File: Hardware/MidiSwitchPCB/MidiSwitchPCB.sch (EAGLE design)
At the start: 78 parts, among them IC3 74LVC2G04GW,125, J1 694108106102, J2 NMJ6HCD2, J3 NMJ6HCD2, J4 NMJ6HCD2, J5 NMJ6HCD2, Q1 BSS123, Q2 BSS123, Q3 BSS123, Q4 BSS123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

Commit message: Continued Layout editing.
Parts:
- C_OUT: device rcl:C-EUC1206 -> rcl:C-EUC1210K
- OK1: value HCPL0500 -> 6N138S; device optocoupler:HCPL0500 -> 6N138S:6N138S
- R20, R21, R22, R23, R24, R25, R26, R27: value (none) -> 61
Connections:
- removed net N$2: U$1.P$1
- removed net N$4: U$1.P$2
- removed net N$6: U$1.P$3
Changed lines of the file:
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@@
 <setting verticaltext="up"/>
 </settings>
-<grid distance="0.01" unitdist="mm" unit="mm" style="lines" multiple="10" display="yes" altdistance="0.01" altunitdist="mm" altunit="mm"/>
+<grid distance="0.01" unitdist="mm" unit="mm" style="lines" multiple="1" display="no" altdistance="0.01" altunitdist="mm" altunit="mm"/>
 <layers>
 <layer number="1" name="Top" color="4" fill="1" visible="no" active="no"/>
@@
 </class>
 <class number="1" name="Power" width="1.016" drill="1.016">
-<clearance class="1" value="0.4064"/>
+<clearance class="1" value="0.8128"/>
 </class>
 <class number="2" name="Signal" width="0.4064" drill="0.6096">
 <clearance class="2" value="0.4064"/>
+</class>
+<class number="3" name="WideIsolation" width="0.4064" drill="1.016">
+<clearance class="3" value="2.032"/>
 </class>
 </classes>
@@
 <part name="U$2" library="MidiSwitchParts" deviceset="MIDI_CONNECTOR" device=""/>
 <part name="U$1" library="MidiSwitchParts" deviceset="MIDI_CONNECTOR" device=""/>
-<part name="OK1" library="optocoupler" deviceset="HCPL0500" device=""/>
+<part name="OK1" library="6N138S" deviceset="6N138S" device=""/>
 <part name="D1" library="diode" deviceset="BAS70" device=""/>
 <part name="R1" library="rcl" deviceset="R-EU_" device="R0603" value="220"/>
@@
 <part name="SUPPLY14" library="supply2" deviceset="GND" device=""/>
 <part name="SUPPLY15" library="supply2" deviceset="GND" device=""/>
-<part name="C_OUT" library="rcl" deviceset="C-EU" device="C1206" value="22µF"/>
+<part name="C_OUT" library="rcl" deviceset="C-EU" device="C1210K" value="22µF"/>
 <part name="SUPPLY16" library="supply2" deviceset="GND" device=""/>
 <part name="C_BST2" library="rcl" deviceset="C-EU" device="C1206" value="100nF"/>
@@
 <part name="R_PWRL_UP" library="rcl" deviceset="R-EU_" device="R0603" value="0R"/>
 <part name="R_PWRL_DOWN" library="rcl" deviceset="R-EU_" device="R0603" value="0R"/>
-<part name="R20" library="rcl" deviceset="R-EU_" device="R0603"/>
-<part name="R21" library="rcl" deviceset="R-EU_" device="R0603"/>
-<part name="R22" library="rcl" deviceset="R-EU_" device="R0603"/>
-<part name="R23" library="rcl" deviceset="R-EU_" device="R0603"/>
-<part name="R24" library="rcl" deviceset="R-EU_" device="R0603"/>
-<part name="R25" library="rcl" deviceset="R-EU_" device="R0603"/>
-<part name="R26" library="rcl" deviceset="R-EU_" device="R0603"/>
-<part name="R27" library="rcl" deviceset="R-EU_" device="R0603"/>
+<part name="R20" library="rcl" deviceset="R-EU_" device="R0603" value="61"/>
+<part name="R21" library="rcl" deviceset="R-EU_" device="R0603" value="61"/>
+<part name="R22" library="rcl" deviceset="R-EU_" device="R0603" value="61"/>
+<part name="R23" library="rcl" deviceset="R-EU_" device="R0603" value="61"/>
+<part name="R24" library="rcl" deviceset="R-EU_" device="R0603" value="61"/>
+<part name="R25" library="rcl" deviceset="R-EU_" device="R0603" value="61"/>
+<part name="R26" library="rcl" deviceset="R-EU_" device="R0603" value="61"/>
+<part name="R27" library="rcl" deviceset="R-EU_" device="R0603" value="61"/>
 <part name="J1" library="SamacSys_Parts" deviceset="694108106102" device=""/>
 <part name="U$3" library="SamacSys_Parts" deviceset="G6L-1F-TR_DC5-NEW" device=""/>
@@
 <instance part="U$2" gate="G$1" x="13.14" y="53.42"/>
 <instance part="U$1" gate="G$1" x="12.5" y="82.6"/>
-<instance part="OK1" gate="A" x="57.82" y="83.54"/>
+<instance part="OK1" gate="G$1" x="57.82" y="83.54"/>
 <instance part="D1" gate="1" x="43.32" y="82.01" rot="R90"/>
 <instance part="R1" gate="G$1" x="37.53" y="88.6"/>
@@
 </busses>
 <nets>
-<net name="N$2" class="0">
-<segment>
-<wire x1="25.5" y1="88.6" x2="27.9" y2="88.6" width="0.1524" layer="91"/>
-<pinref part="U$1" gate="G$1" pin="P$1"/>
-</segment>
-</net>
-<net name="N$4" class="0">
-<segment>
-<wire x1="25.5" y1="82.6" x2="28.1" y2="82.6" width="0.1524" layer="91"/>
-<pinref part="U$1" gate="G$1" pin="P$2"/>
-</segment>
-</net>
-<net name="N$6" class="0">
-<segment>
-<wire x1="25.5" y1="76.6" x2="28.3" y2="76.6" width="0.1524" layer="91"/>
-<pinref part="U$1" gate="G$1" pin="P$3"/>
-</segment>
-</net>
-<net name="N$3" class="0">
+<net name="N$3" class="3">
 <segment>
 <pinref part="U$1" gate="G$1" pin="P$4"/>
@@
 <net name="N$7" class="0">
 <segment>
-<pinref part="OK1" gate="A" pin="A"/>
+<pinref part="OK1" gate="G$1" pin="A"/>
 <wire x1="43.32" y1="84.55" x2="43.34" y2="88.6" width="0.1524" layer="91"/>
 <wire x1="43.34" y1="88.6" x2="45.12" y2="88.62" width="0.1524" layer="91"/>
@@
 </segment>
 </net>
-<net name="N$8" class="0">
+<net name="N$8" class="3">
 <segment>
 <wire x1="45.12" y1="78.46" x2="43.33" y2="78.44" width="0.1524" layer="91"/>
@@
 <wire x1="43.33" y1="78.44" x2="32.82" y2="78.44" width="0.1524" layer="91"/>
 <wire x1="32.82" y1="78.44" x2="31.55" y2="79.56" width="0.1524" layer="91"/>
-<pinref part="OK1" gate="A" pin="C"/>
+<pinref part="OK1" gate="G$1" pin="C"/>
 <junction x="43.33" y="78.44"/>
 <pinref part="D1" gate="1" pin="A"/>
@@
 <net name="MIDI_RX" class="0">
 <segment>
-<pinref part="OK1" gate="A" pin="VB"/>
+<pinref part="OK1" gate="G$1" pin="VB"/>
 <pinref part="R2" gate="G$1" pin="2"/>
-<wire x1="67.98" y1="86.08" x2="80.37" y2="86.07" width="0.1524" layer="91"/>
+<wire x1="70.52" y1="86.08" x2="80.37" y2="86.07" width="0.1524" layer="91"/>
 <wire x1="80.37" y1="86.07" x2="80.37" y2="85.37" width="0.1524" layer="91"/>
 <wire x1="86.48" y1="86.07" x2="80.37" y2="86.07" width="0.1524" layer="91"/>
@@
 <net name="N$9" class="0">
 <segment>
-<pinref part="OK1" gate="A" pin="VO"/>
+<pinref part="OK1" gate="G$1" pin="VO"/>
 <pinref part="R3" gate="G$1" pin="1"/>
-<wire x1="67.98" y1="83.54" x2="75.44" y2="83.54" width="0.1524" layer="91"/>
+<wire x1="70.52" y1="83.54" x2="75.44" y2="83.54" width="0.1524" layer="91"/>
 <wire x1="75.44" y1="83.54" x2="88.47" y2="83.58" width="0.1524" layer="91"/>
 <wire x1="88.47" y1="83.58" x2="103.89" y2="83.58" width="0.1524" layer="91"/>
 <pinref part="CN7" gate="A" pin="3"/>
 <wire x1="103.89" y1="83.58" x2="103.94" y2="93.07" width="0.1524" layer="91"/>
+<junction x="75.44" y="83.54"/>
 </segment>
 </net>
@@
 <wire x1="80.37" y1="75.21" x2="72.64" y2="75.21" width="0.1524" layer="91"/>
 <pinref part="SUPPLY1" gate="GND" pin="GND"/>
-<pinref part="OK1" gate="A" pin="GND"/>
-<wire x1="67.98" y1="78.46" x2="72.64" y2="78.46" width="0.1524" layer="91"/>
+<pinref part="OK1" gate="G$1" pin="GND"/>
+<wire x1="70.52" y1="78.46" x2="72.64" y2="78.46" width="0.1524" layer="91"/>
 <junction x="72.64" y="75.2"/>
 </segment>
@@
 <pinref part="U$1" gate="G$1" pin="P$6"/>
 <pinref part="SUPPLY2" gate="GND" pin="GND"/>
+<junction x="29.5" y="73.61"/>
 </segment>
 <segment>
@@
 <net name="VCC_3_3" class="0">
 <segment>
-<pinref part="OK1" gate="A" pin="VCC"/>
-<wire x1="67.98" y1="88.62" x2="67.98" y2="94.64" width="0.1524" layer="91"/>
+<pinref part="OK1" gate="G$1" pin="VCC"/>
+<wire x1="70.52" y1="88.62" x2="70.46" y2="90.84" width="0.1524" layer="91"/>
 <pinref part="R3" gate="G$1" pin="2"/>
-<wire x1="67.98" y1="94.64" x2="70.52" y2="94.64" width="0.1524" layer="91"/>
+<wire x1="70.46" y1="90.84" x2="70.52" y2="94.64" width="0.1524" layer="91"/>
 <wire x1="70.52" y1="94.64" x2="75.44" y2="94.64" width="0.1524" layer="91"/>
 <wire x1="75.44" y1="94.64" x2="75.44" y2="93.7" width="0.1524" layer="91"/>
@@
 </segment>
 </net>
-<net name="N$66" class="0">
+<net name="N$66" class="1">
 <segment>
 <pinref part="F1" gate="G$1" pin="2"/>
@@
 </sheet>
 </sheets>
+<errors>
+</errors>
 </schematic>
 </drawing>

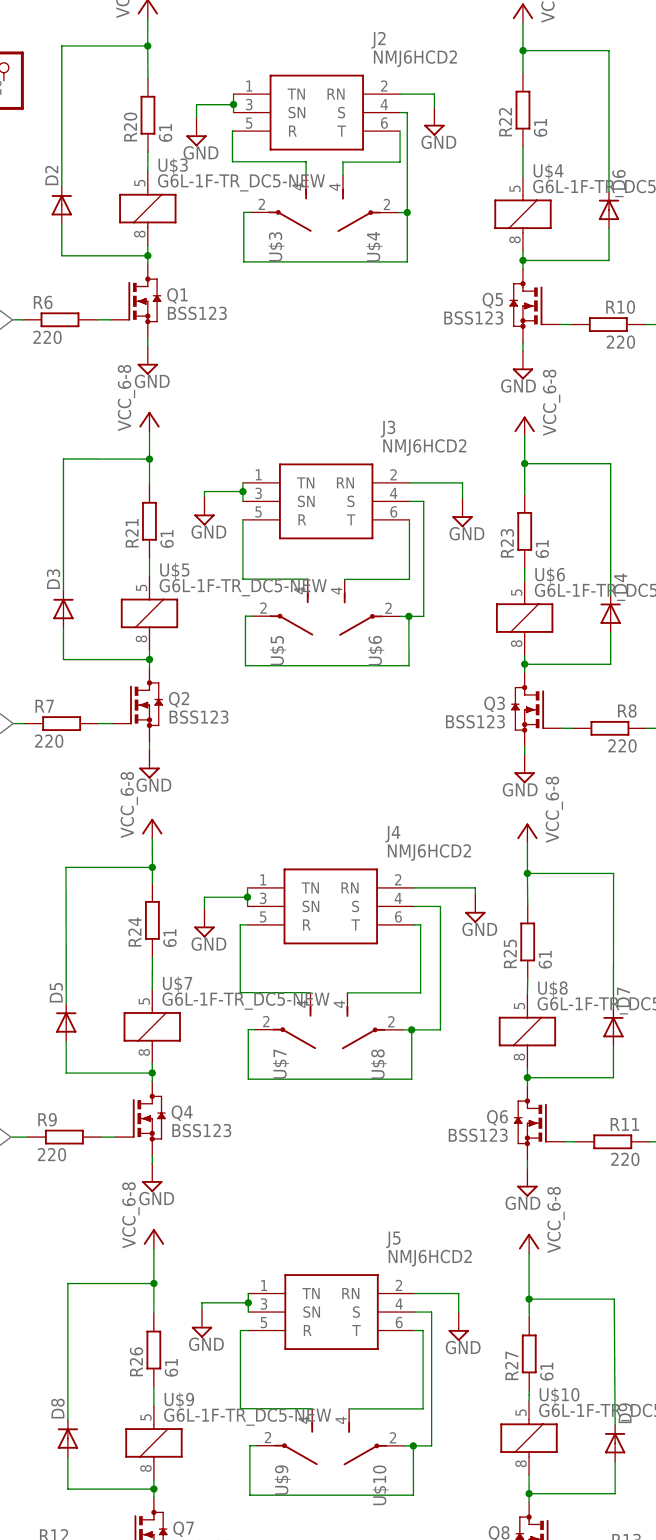
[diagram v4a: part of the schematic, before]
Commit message: Changed PCB size to 160 x 100
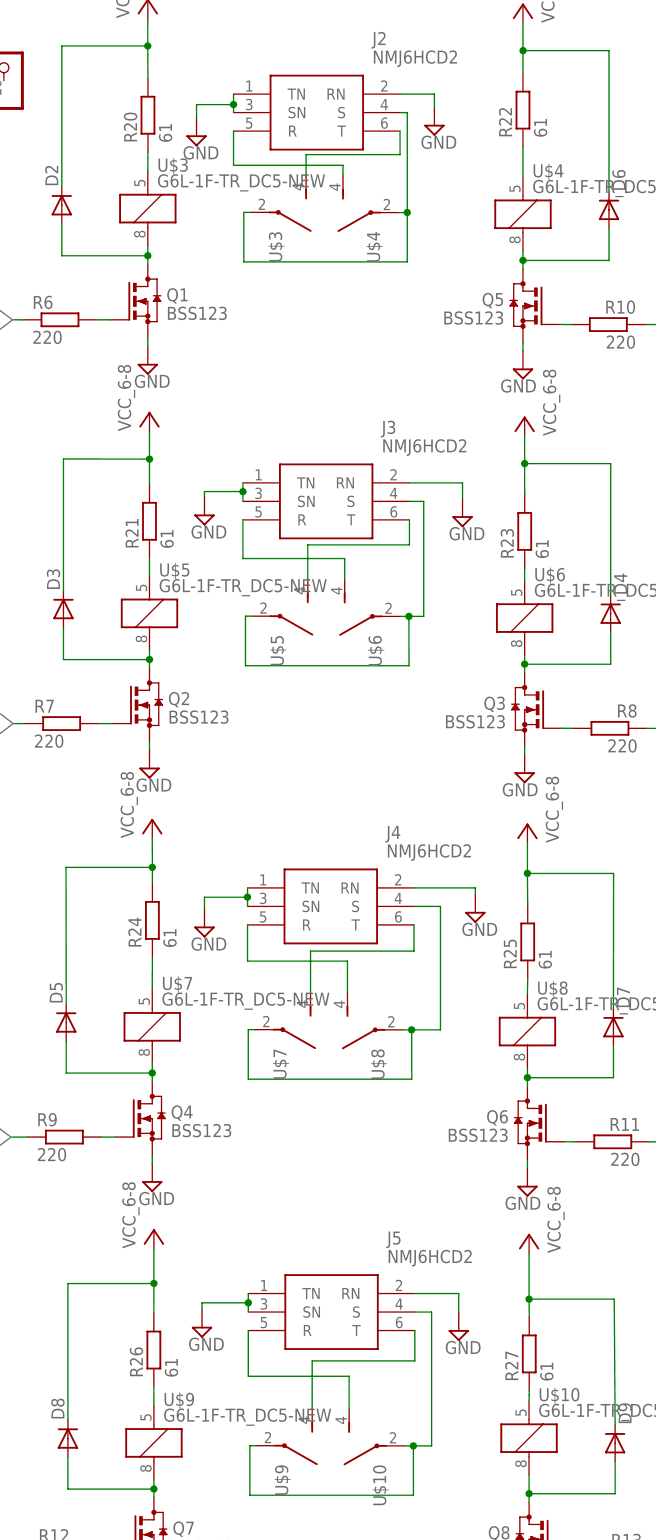
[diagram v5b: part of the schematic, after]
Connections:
- removed net N$36: J2.R, U$3G$2.S
- removed net N$37: J2.T, U$4G$2.S
- removed net N$41: J5.R, U$9G$2.S
- removed net N$50: J5.T, U$10G$2.S
- new net N$2: J2.T, U$3G$2.S
- new net N$28: J4.R, U$8G$2.S
- new net N$4: J2.R, U$4G$2.S
- new net N$6: J3.T, U$5G$2.S
- net N$19: now also U$6G$2.S; no longer U$5G$2.S
- net N$22: now also J4.T, U$7G$2.S; no longer J3.T, U$6G$2.S
- net N$29: now also J5.T, U$9G$2.S; no longer J4.T, U$8G$2.S
- net N$30: now also J5.R, U$10G$2.S; no longer J4.R, U$7G$2.S

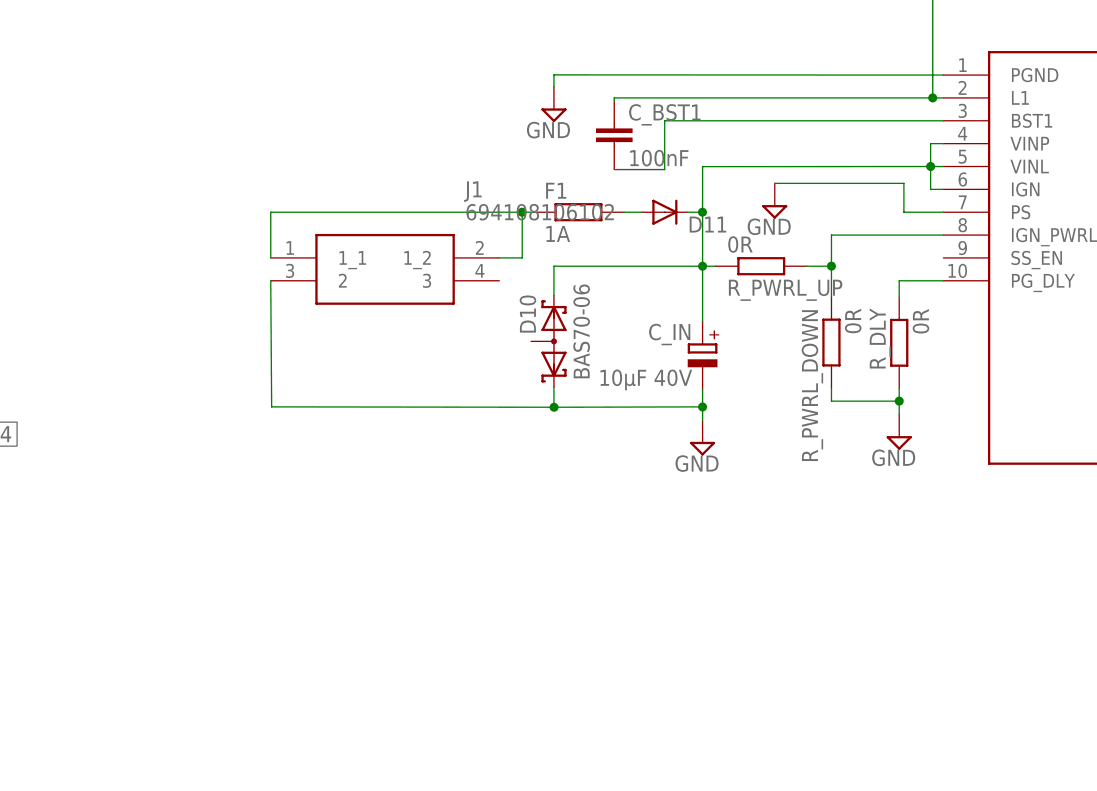
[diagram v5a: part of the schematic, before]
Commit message: Started reworking the layout before ordering it
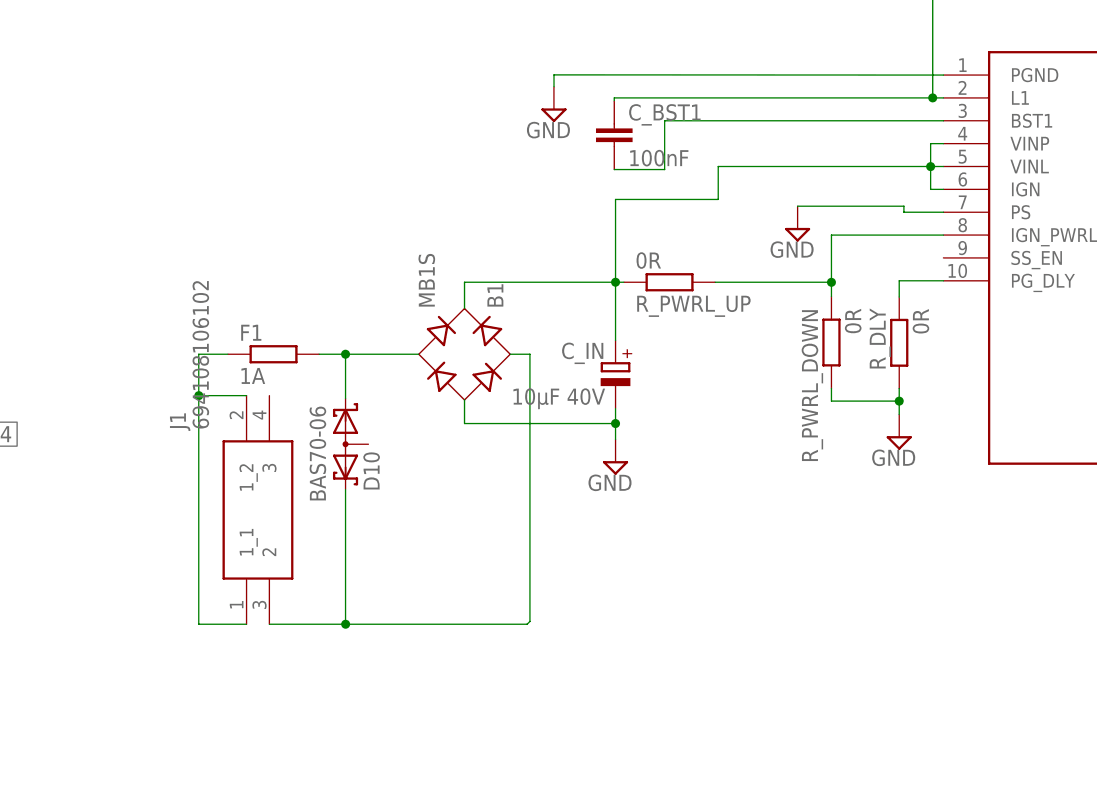
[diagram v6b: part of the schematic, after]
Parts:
- removed D11: (no value), diode:DIODE-DO-214AC
- added B1: MB1S, rectifier:MB1S
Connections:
- removed net N$66: D11.A, F1.2
- removed net VIN: F1.1, J1.1_1
- removed net VIN_FUSED: C_IN.+, D10.K2, D11.C, PS1.IGN, PS1.VINL, PS1.VINP, R_PWRL_UP.1
- new net N$36: B1.AC2, D10.K1, F1.2
- new net N$37: B1.AC1, D10.K2, J1.2
- new net N$40: F1.1, J1.1_1, J1.1_2
- new net N$41: B1.+, C_IN.+, PS1.IGN, PS1.VINL, PS1.VINP, R_PWRL_UP.1
- net GND: now also B1.-; no longer D10.K1, J1.2
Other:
- moved on the sheet: C_IN, D10, F1, J1, R_PWRL_UP
